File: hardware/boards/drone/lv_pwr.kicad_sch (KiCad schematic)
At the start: 20 parts, among them U10 AP63356QZV-7, U13 INA2180A3IDSGR, U9 AP63356QZV-7

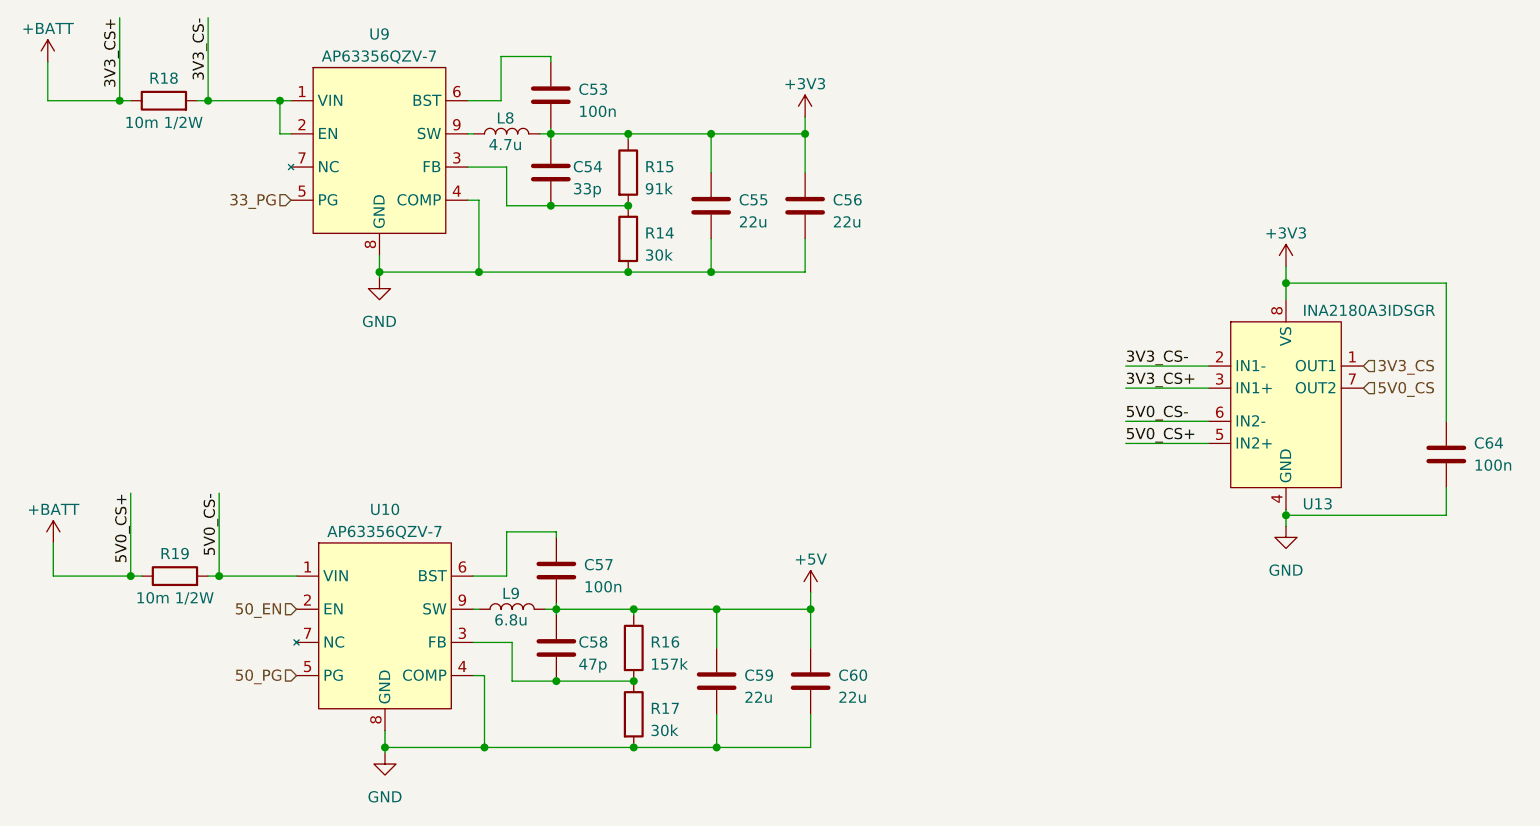
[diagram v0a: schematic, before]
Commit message: Added Power & Charging Subsystems
- Replaced Qi receiver
- Added charge controller
- Added BMS
- Added switch between Qi & USB-PD
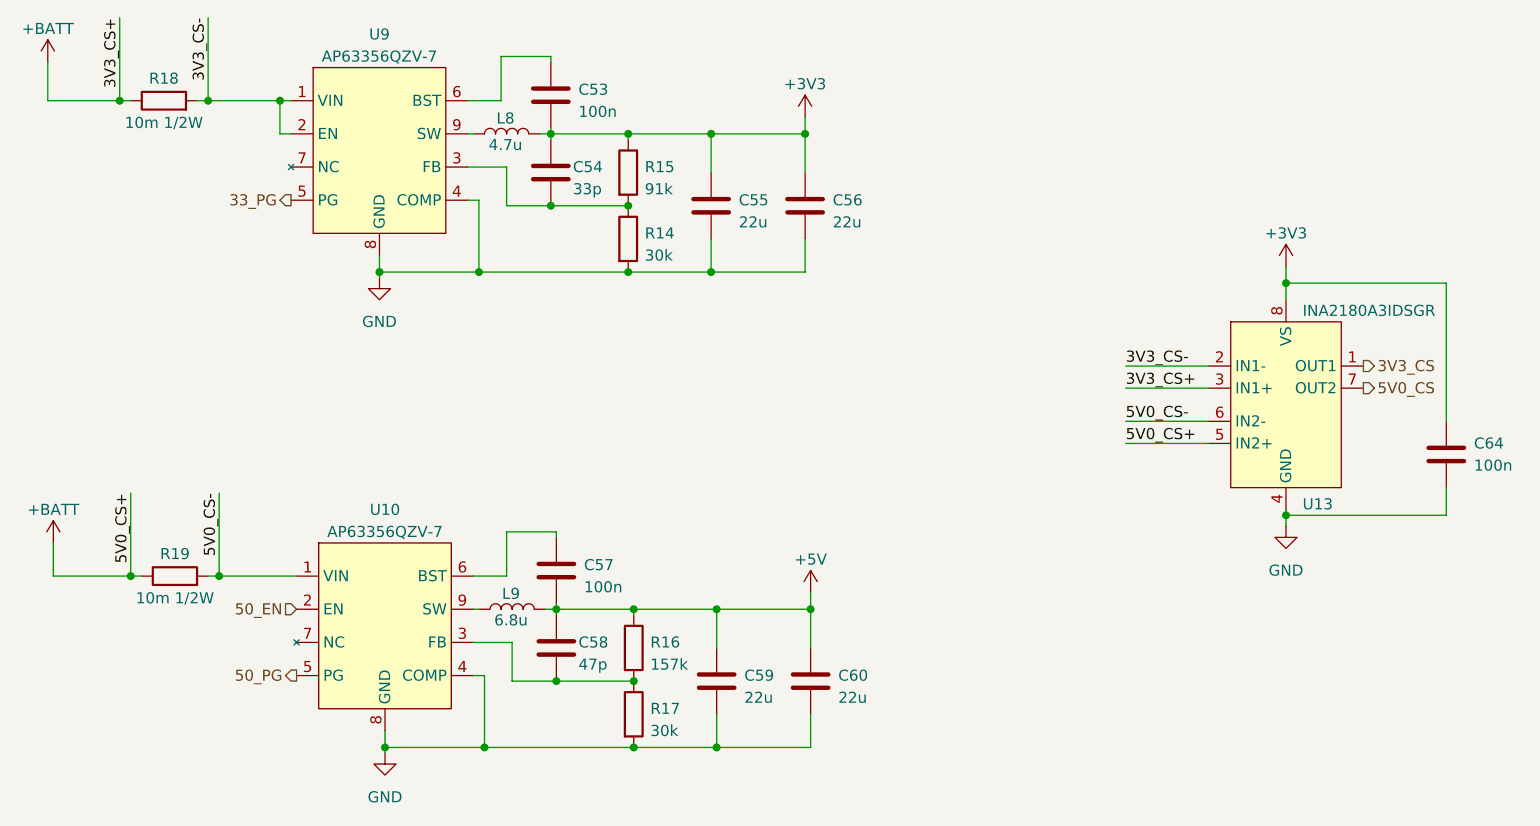
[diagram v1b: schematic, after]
